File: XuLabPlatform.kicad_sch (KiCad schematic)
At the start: 12 parts, among them J10 Servo7, J11 Servo8, J12 Thruster SGN, J14 CAN, J15 I2C, J16 UART, J4 Servo1, J5 Servo2, J6 Servo3, J7 Servo4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

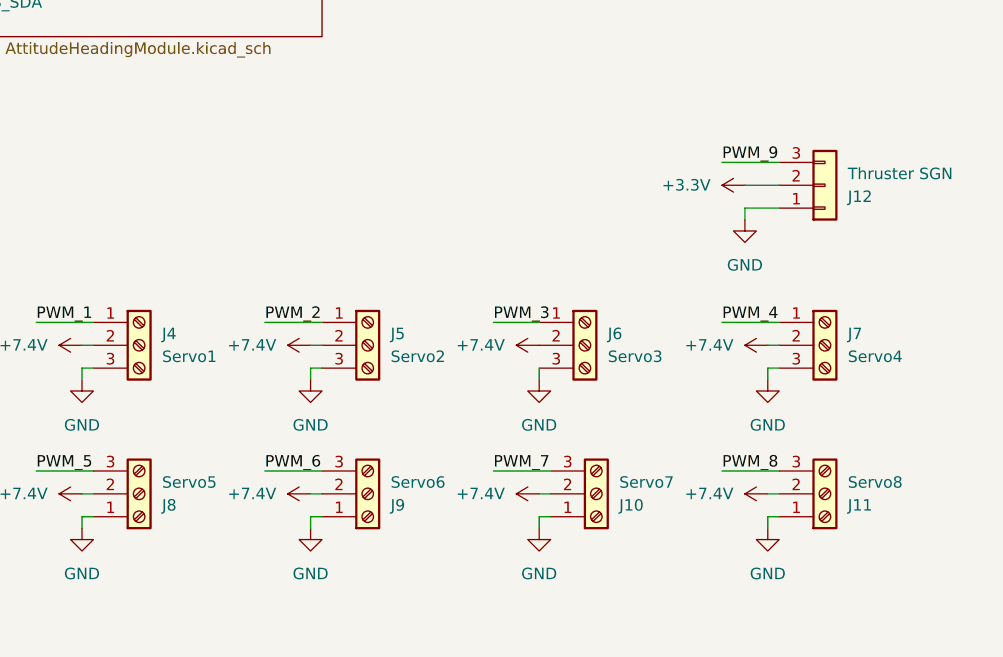
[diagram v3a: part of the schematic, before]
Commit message: Add interchangeable field to BOM
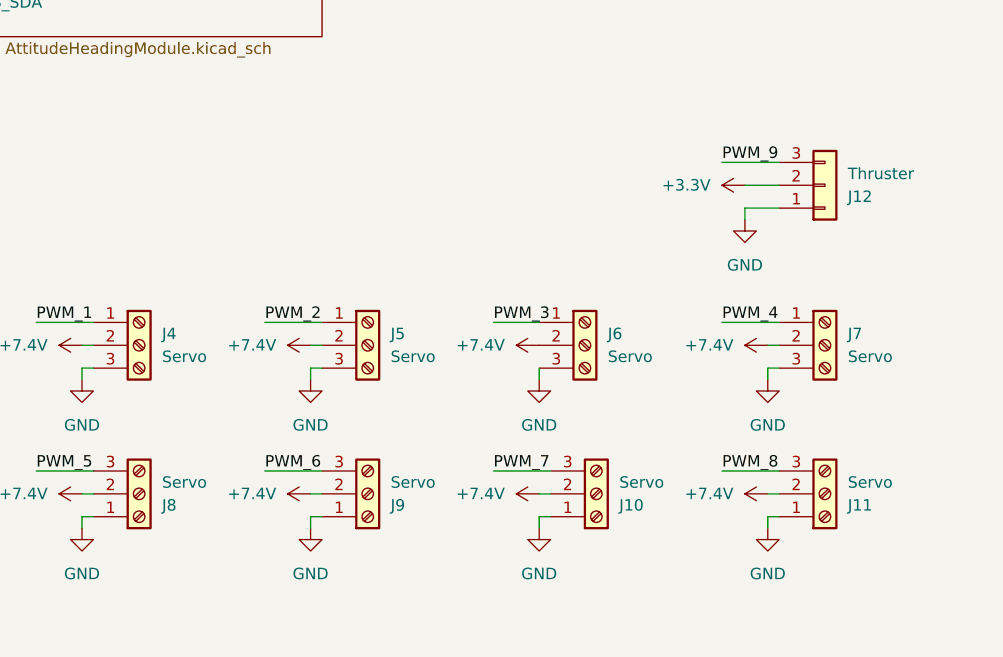
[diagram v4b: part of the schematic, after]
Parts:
- J10: value Servo7 -> Servo; Interchangeable (none) -> No
- J11: value Servo8 -> Servo; Interchangeable (none) -> No
- J12: value Thruster SGN -> Thruster; Interchangeable (none) -> No
- J14, J15, J16: Interchangeable (none) -> Yes; Listing (none) -> https://www.digikey.com/en/products/detail/sullins-connecto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
- J4: value Servo1 -> Servo; Interchangeable (none) -> No
- J5: value Servo2 -> Servo; Interchangeable (none) -> No
- J6: value Servo3 -> Servo; Interchangeable (none) -> No
- J7: value Servo4 -> Servo; Interchangeable (none) -> No
- J8: value Servo5 -> Servo; Interchangeable (none) -> No
- J9: value Servo6 -> Servo; Interchangeable (none) -> No
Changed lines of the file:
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@@
 			)
 		)
-		(property "Datasheet" ""
+		(property "Datasheet" "https://drawings-pdf.s3.amazonaws.com/10483.pdf"
 			(at 265.43 29.21 0)
 			(effects
@@
 			)
 		)
-		(property "Listing" ""
+		(property "Listing" "https://www.digikey.com/en/products/detail/sullins-connector-solutions/NPPN031BFCN-RC/804805"
+			(at 265.43 29.21 0)
+			(effects
+				(font
+					(size 1.27 1.27)
+				)
+				(hide yes)
+			)
+		)
+		(property "Interchangeable" "Yes"
 			(at 265.43 29.21 0)
 			(effects
@@
 			)
 		)
-		(property "Value" "Servo6"
+		(property "Value" "Servo"
 			(at 217.17 144.7801 0)
 			(effects
@@
 			)
 		)
+		(property "Interchangeable" "No"
+			(at 214.63 146.05 0)
+			(effects
+				(font
+					(size 1.27 1.27)
+				)
+				(hide yes)
+			)
+		)
 		(pin "1"
 		)
@@
 			)
 		)
-		(property "Value" "Servo1"
+		(property "Value" "Servo"
 			(at 191.77 130.8099 0)
 			(effects
@@
 			)
 		)
+		(property "Interchangeable" "No"
+			(at 189.23 129.54 0)
+			(effects
+				(font
+					(size 1.27 1.27)
+				)
+				(hide yes)
+			)
+		)
 		(pin "1"
 		)
@@
 			)
 		)
-		(property "Datasheet" ""
+		(property "Datasheet" "https://drawings-pdf.s3.amazonaws.com/10483.pdf"
 			(at 265.43 48.26 0)
 			(effects
@@
 			)
 		)
-		(property "Listing" ""
+		(property "Listing" "https://www.digikey.com/en/products/detail/sullins-connector-solutions/NPPN031BFCN-RC/804805"
+			(at 265.43 48.26 0)
+			(effects
+				(font
+					(size 1.27 1.27)
+				)
+				(hide yes)
+			)
+		)
+		(property "Interchangeable" "Yes"
 			(at 265.43 48.26 0)
 			(effects
@@
 			)
 		)
-		(property "Value" "Servo5"
+		(property "Value" "Servo"
 			(at 191.77 144.7801 0)
 			(effects
@@
 		)
 		(property "Listing" "https://www.digikey.com/en/products/detail/phoenix-contact/1715734/260632"
+			(at 189.23 146.05 0)
+			(effects
+				(font
+					(size 1.27 1.27)
+				)
+				(hide yes)
+			)
+		)
+		(property "Interchangeable" "No"
 			(at 189.23 146.05 0)
 			(effects
@@
 			)
 		)
-		(property "Value" "Servo7"
+		(property "Value" "Servo"
 			(at 242.57 144.7801 0)
 			(effects
@@
 			)
 		)
+		(property "Interchangeable" "No"
+			(at 240.03 146.05 0)
+			(effects
+				(font
+					(size 1.27 1.27)
+				)
+				(hide yes)
+			)
+		)
 		(pin "1"
 		)
@@
 			)
 		)
-		(property "Value" "Servo2"
+		(property "Value" "Servo"
 			(at 217.17 130.8099 0)
 			(effects
@@
 			)
 		)
+		(property "Interchangeable" "No"
+			(at 214.63 129.54 0)
+			(effects
+				(font
+					(size 1.27 1.27)
+				)
+				(hide yes)
+			)
+		)
 		(pin "1"
 		)
@@
 			)
 		)
-		(property "Datasheet" ""
+		(property "Datasheet" "https://drawings-pdf.s3.amazonaws.com/10483.pdf"
 			(at 265.43 67.31 0)
 			(effects
@@
 			)
 		)
-		(property "Listing" ""
+		(property "Listing" "https://www.digikey.com/en/products/detail/sullins-connector-solutions/NPPN031BFCN-RC/804805"
+			(at 265.43 67.31 0)
+			(effects
+				(font
+					(size 1.27 1.27)
+				)
+				(hide yes)
+			)
+		)
+		(property "Interchangeable" "Yes"
 			(at 265.43 67.31 0)
 			(effects
@@
 			)
 		)
-		(property "Value" "Servo4"
+		(property "Value" "Servo"
 			(at 267.97 130.8099 0)
 			(effects
@@
 			)
 		)
+		(property "Interchangeable" "No"
+			(at 265.43 129.54 0)
+			(effects
+				(font
+					(size 1.27 1.27)
+				)
+				(hide yes)
+			)
+		)
 		(pin "1"
 		)
@@
 			)
 		)
-		(property "Value" "Servo3"
+		(property "Value" "Servo"
 			(at 241.3 130.8099 0)
 			(effects
@@
 		)
 		(property "Listing" "https://www.digikey.com/en/products/detail/phoenix-contact/1715734/260632"
+			(at 238.76 129.54 0)
+			(effects
+				(font
+					(size 1.27 1.27)
+				)
+				(hide yes)
+			)
+		)
+		(property "Interchangeable" "No"
 			(at 238.76 129.54 0)
 			(effects
@@
 			)
 		)
-		(property "Value" "Thruster SGN"
+		(property "Value" "Thruster"
 			(at 267.97 110.4901 0)
 			(effects
@@
 		)
 		(property "Listing" "https://www.digikey.com/en/products/detail/jst-sales-america-inc/B3P-VH/926548"
+			(at 265.43 111.76 0)
+			(effects
+				(font
+					(size 1.27 1.27)
+				)
+				(hide yes)
+			)
+		)
+		(property "Interchangeable" "No"
 			(at 265.43 111.76 0)
 			(effects
@@
 			)
 		)
-		(property "Value" "Servo8"
+		(property "Value" "Servo"
 			(at 267.97 144.7801 0)
 			(effects
@@
 			(at 265.43 146.05 0)
 			(effects
+				(font
+					(size 1.27 1.27)
+				)
+				(hide yes)
+			)
+		)
+		(property "Interchangeable" "No"
+			(at 265.43 146.05 0)
+			(effects

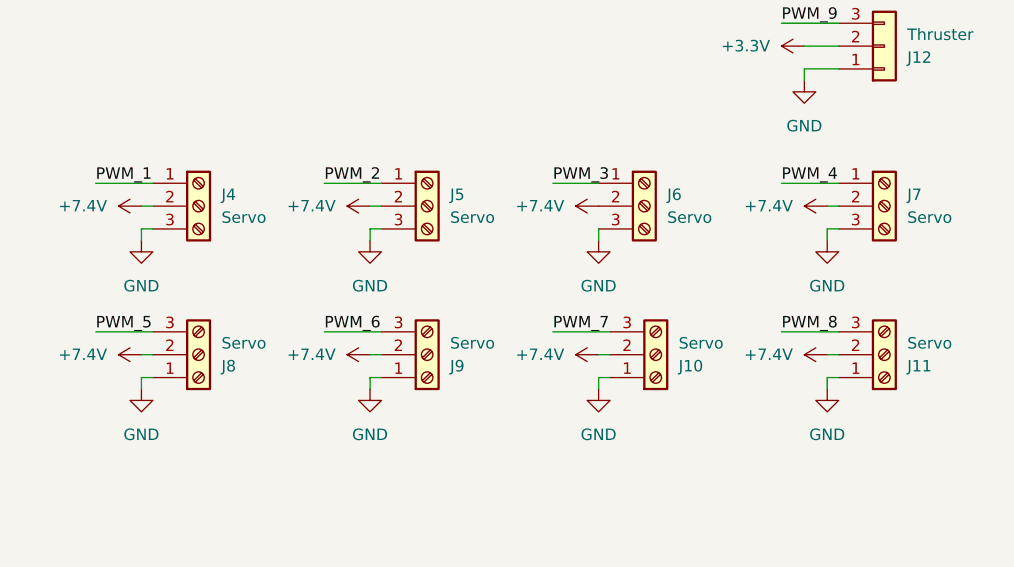
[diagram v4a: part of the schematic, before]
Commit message: Change servo connectors from screw to JST B3P-VH
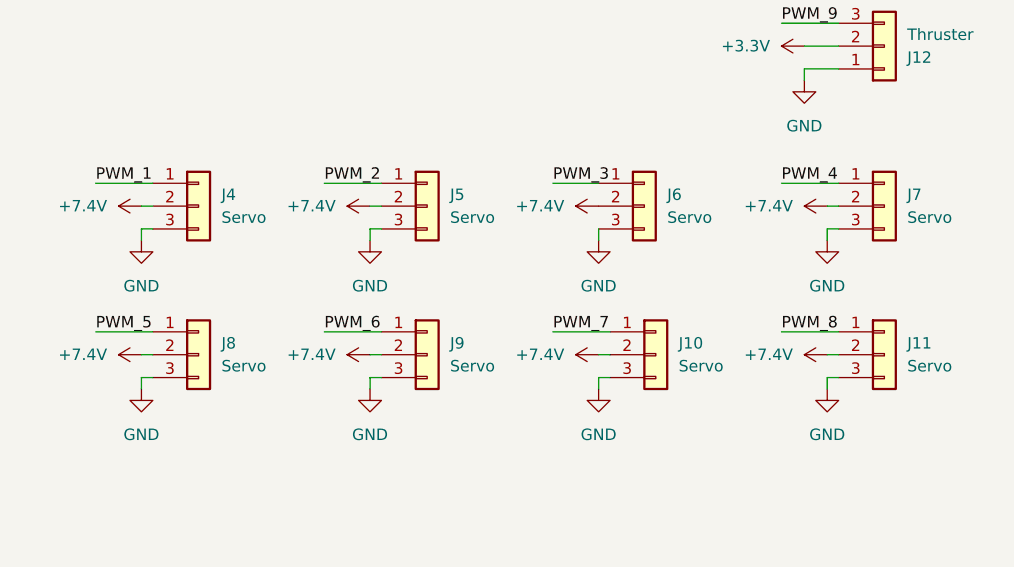
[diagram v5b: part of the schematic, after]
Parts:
- removed J10, J11, J4, J5, J6, J7, J8, J9: Servo, TerminalBlock_Phoenix:TerminalBlock_Phoenix_MKDS-1,5-3-5.08_1x03_P5.08mm_Horizontal, symbol Connector:Screw_Terminal_01x03
- added J10, J11, J4, J5, J6, J7, J8, J9: Servo, Connector_JST:JST_VH_B3P-VH-B_1x03_P3.96mm_Vertical, symbol Connector_Generic:Conn_01x03
- J12: footprint Connector_JST:JST_VH_B3P-VH_1x03_P3.96mm_Vertical -> Connector_JST:JST_VH_B3P-VH-B_1x03_P3.96mm_Vertical
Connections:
- net +7.4V: now also J10.2 (Pin_2), J11.2 (Pin_2), J4.2 (Pin_2), J5.2 (Pin_2), J6.2 (Pin_2), J7.2 (Pin_2), J8.2 (Pin_2), J9.2 (Pin_2)
- net GND: now also J10.3 (Pin_3), J11.3 (Pin_3), J4.3 (Pin_3), J5.3 (Pin_3), J6.3 (Pin_3), J7.3 (Pin_3), J8.3 (Pin_3), J9.3 (Pin_3)
- net PWM_1: now also J4.1 (Pin_1)
- net PWM_2: now also J5.1 (Pin_1)
- net PWM_3: now also J6.1 (Pin_1)
- net PWM_4: now also J7.1 (Pin_1)
- net PWM_5: now also J8.1 (Pin_1)
- net PWM_6: now also J9.1 (Pin_1)
- net PWM_7: now also J10.1 (Pin_1)
- net PWM_8: now also J11.1 (Pin_1)

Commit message: Change output peripheral output connectors to Molex PicoBlade
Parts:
- J14, J15, J16: footprint Connector_PinSocket_2.00mm:PinSocket_1x03_P2.00mm_Vertical -> Connector_Molex:Molex_PicoBlade_53048-0310_1x03_P1.25mm_Horizontal; Interchangeable Yes -> No; Listing https://www.digikey.com/en/products/detail/sullins-connecto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 -> https://www.digikey.com/en/products/detail/molex/0530480310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
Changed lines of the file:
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@@
 	(title_block
 		(title "Main Sheet")
-		(date "2025-12-21")
-		(rev "A")
+		(date "2026-01-25")
+		(rev "B")
 		(company "CU Boulder Senior Design Team 29 - Xu Lab")
 	)
@@
 			)
 		)
-		(property "Footprint" "Connector_PinSocket_2.00mm:PinSocket_1x03_P2.00mm_Vertical"
+		(property "Footprint" "Connector_Molex:Molex_PicoBlade_53048-0310_1x03_P1.25mm_Horizontal"
 			(at 265.43 29.21 0)
 			(effects
@@
 			)
 		)
-		(property "Datasheet" "https://drawings-pdf.s3.amazonaws.com/10483.pdf"
+		(property "Datasheet" "https://www.molex.com/content/dam/molex/molex-dot-com/products/automated/en-us/salesdrawingpdf/530/53048/530480310_sd.pdf?inline"
 			(at 265.43 29.21 0)
 			(effects
@@
 			)
 		)
-		(property "Listing" "https://www.digikey.com/en/products/detail/sullins-connector-solutions/NPPN031BFCN-RC/804805"
+		(property "Listing" "https://www.digikey.com/en/products/detail/molex/0530480310/242865"
 			(at 265.43 29.21 0)
 			(effects
@@
 			)
 		)
-		(property "Interchangeable" "Yes"
+		(property "Interchangeable" "No"
 			(at 265.43 29.21 0)
 			(effects
@@
 			)
 		)
-		(property "Footprint" "Connector_PinSocket_2.00mm:PinSocket_1x03_P2.00mm_Vertical"
+		(property "Footprint" "Connector_Molex:Molex_PicoBlade_53048-0310_1x03_P1.25mm_Horizontal"
 			(at 265.43 48.26 0)
 			(effects
@@
 			)
 		)
-		(property "Datasheet" "https://drawings-pdf.s3.amazonaws.com/10483.pdf"
+		(property "Datasheet" "https://www.molex.com/content/dam/molex/molex-dot-com/products/automated/en-us/salesdrawingpdf/530/53048/530480310_sd.pdf?inline"
 			(at 265.43 48.26 0)
 			(effects
@@
 			)
 		)
-		(property "Listing" "https://www.digikey.com/en/products/detail/sullins-connector-solutions/NPPN031BFCN-RC/804805"
+		(property "Listing" "https://www.digikey.com/en/products/detail/molex/0530480310/242865"
 			(at 265.43 48.26 0)
 			(effects
@@
 			)
 		)
-		(property "Interchangeable" "Yes"
+		(property "Interchangeable" "No"
 			(at 265.43 48.26 0)
 			(effects
@@
 			)
 		)
-		(property "Footprint" "Connector_PinSocket_2.00mm:PinSocket_1x03_P2.00mm_Vertical"
+		(property "Footprint" "Connector_Molex:Molex_PicoBlade_53048-0310_1x03_P1.25mm_Horizontal"
 			(at 265.43 67.31 0)
 			(effects
@@
 			)
 		)
-		(property "Datasheet" "https://drawings-pdf.s3.amazonaws.com/10483.pdf"
+		(property "Datasheet" "https://www.molex.com/content/dam/molex/molex-dot-com/products/automated/en-us/salesdrawingpdf/530/53048/530480310_sd.pdf?inline"
 			(at 265.43 67.31 0)
 			(effects
@@
 			)
 		)
-		(property "Listing" "https://www.digikey.com/en/products/detail/sullins-connector-solutions/NPPN031BFCN-RC/804805"
+		(property "Listing" "https://www.digikey.com/en/products/detail/molex/0530480310/242865"
 			(at 265.43 67.31 0)
 			(effects
@@
 			)
 		)
-		(property "Interchangeable" "Yes"
+		(property "Interchangeable" "No"
 			(at 265.43 67.31 0)
 			(effects

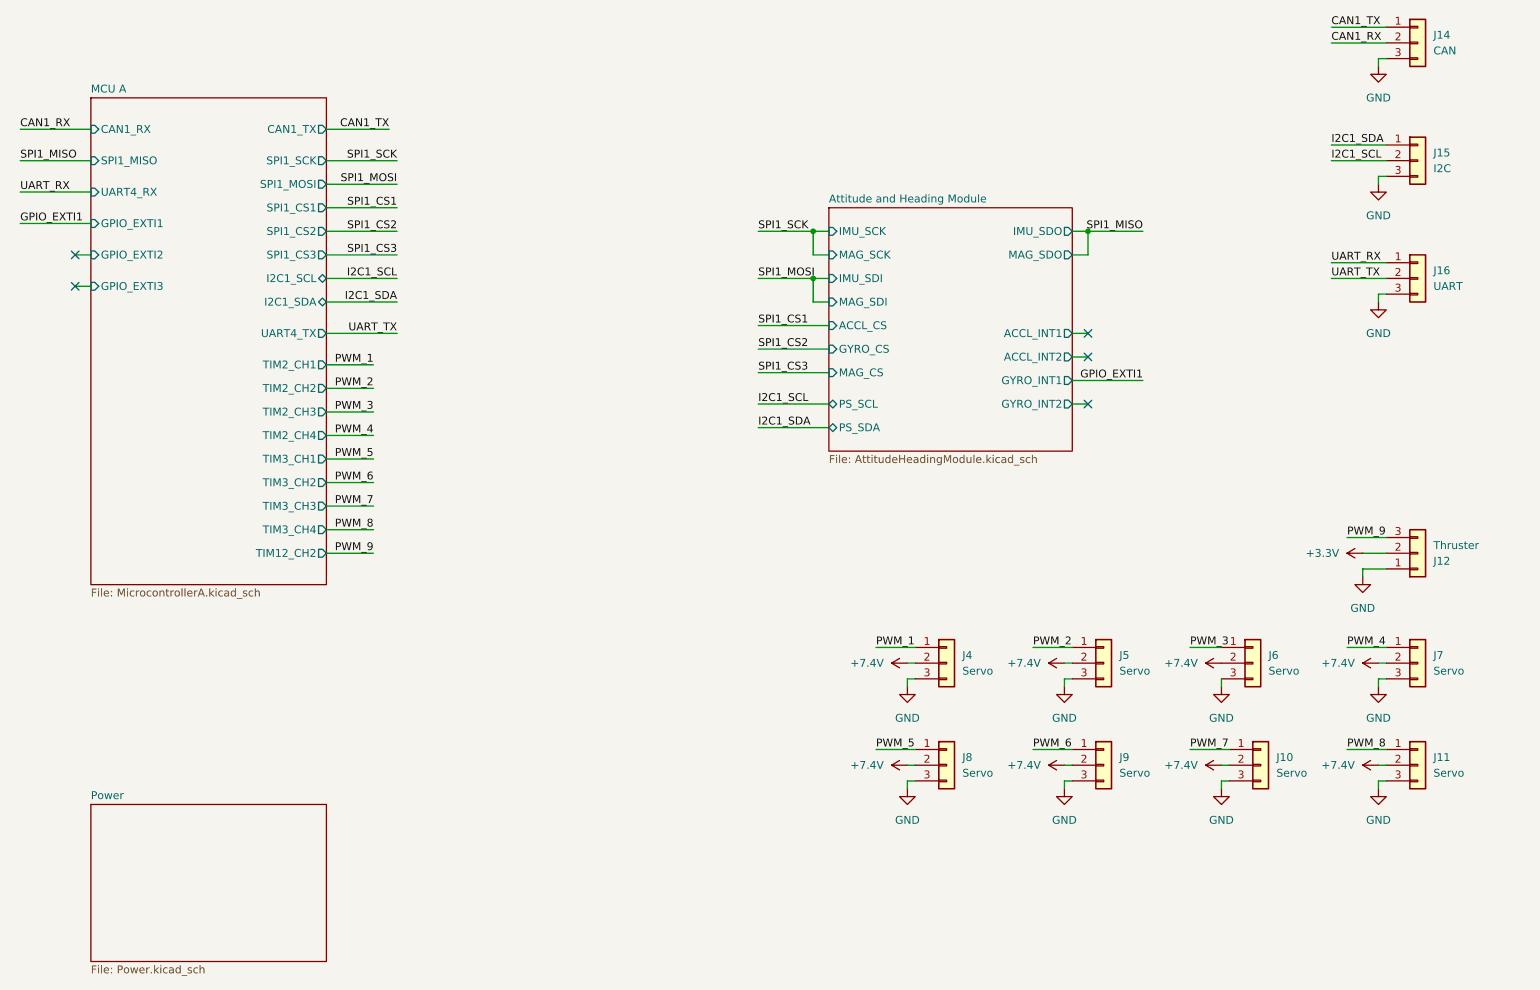
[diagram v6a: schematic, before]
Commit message: Remove CAN pins and connector
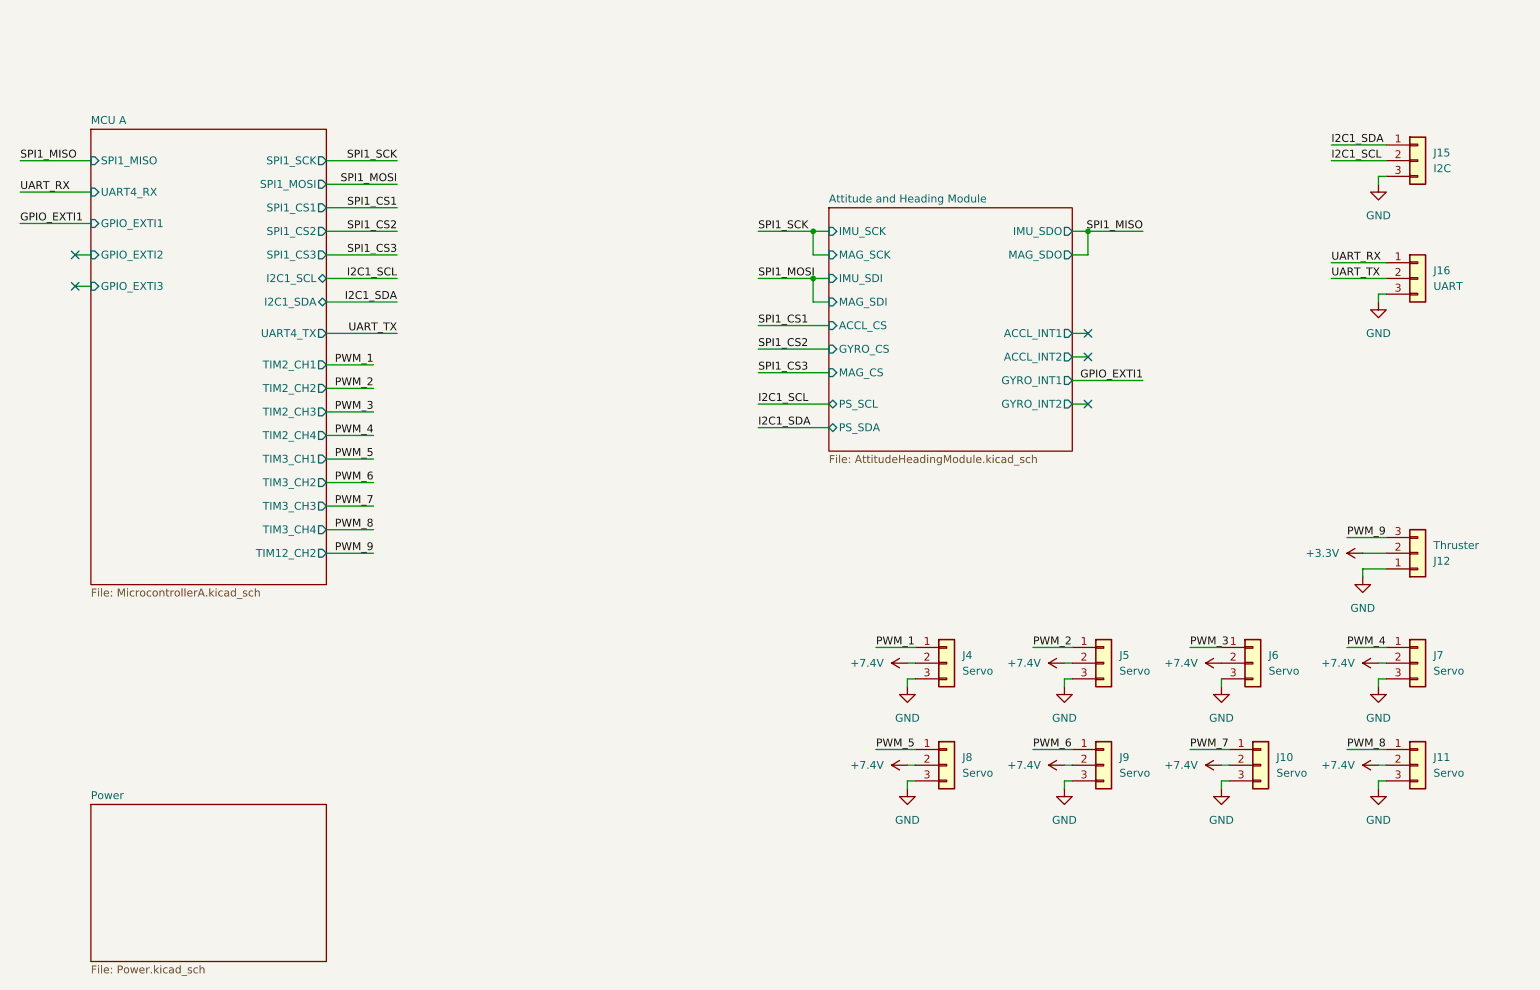
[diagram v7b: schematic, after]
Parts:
- removed J14: CAN, Connector_Molex:Molex_PicoBlade_53048-0310_1x03_P1.25mm_Horizontal, symbol Connector_Generic:Conn_01x03
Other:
- sheet MCU A ports: added none; removed CAN1_RX, CAN1_TX
